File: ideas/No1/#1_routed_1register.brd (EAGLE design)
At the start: 110.2 x 90.1 mm, 20 parts, among them P1-O8RIGHT TD627832A, P1-P8LEFT TD627832A, U1 SN74HC595N, U2 SN74HC595N, U3 SN74HC595N

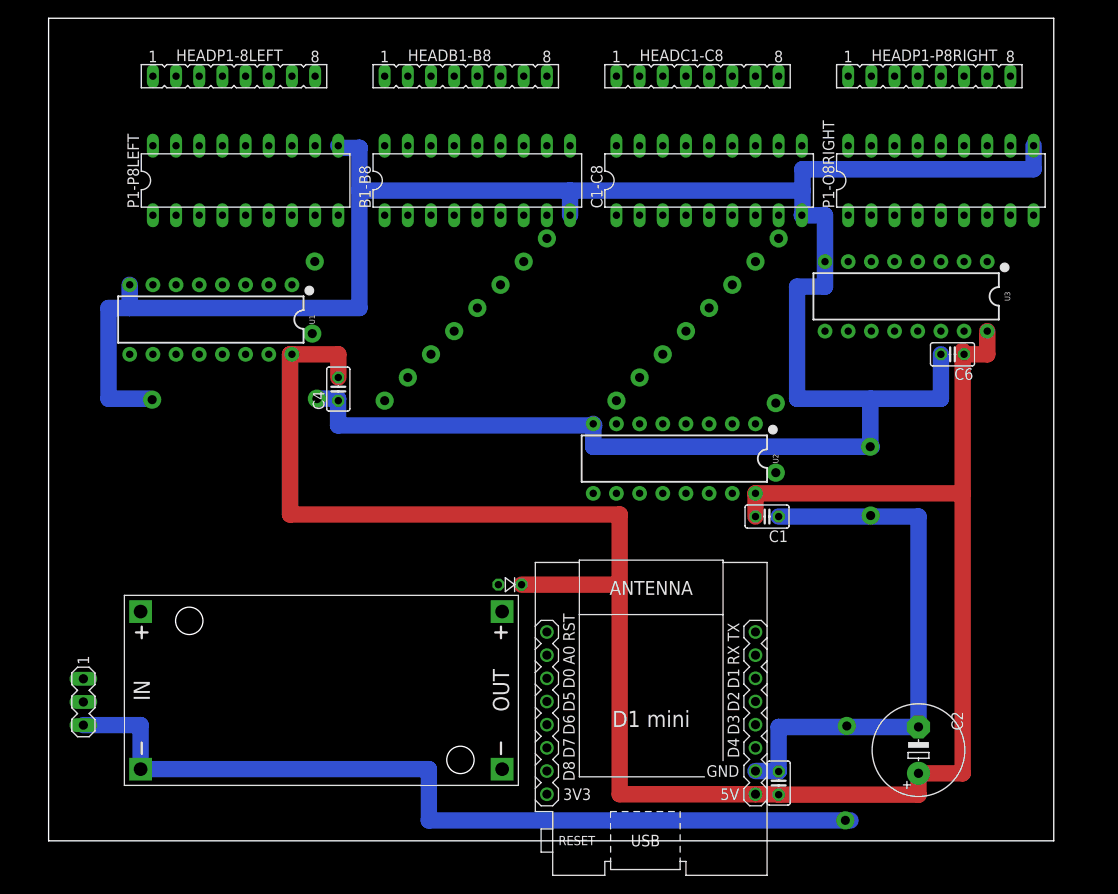
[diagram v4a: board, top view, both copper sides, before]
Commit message: 1_route_1register.sch changed
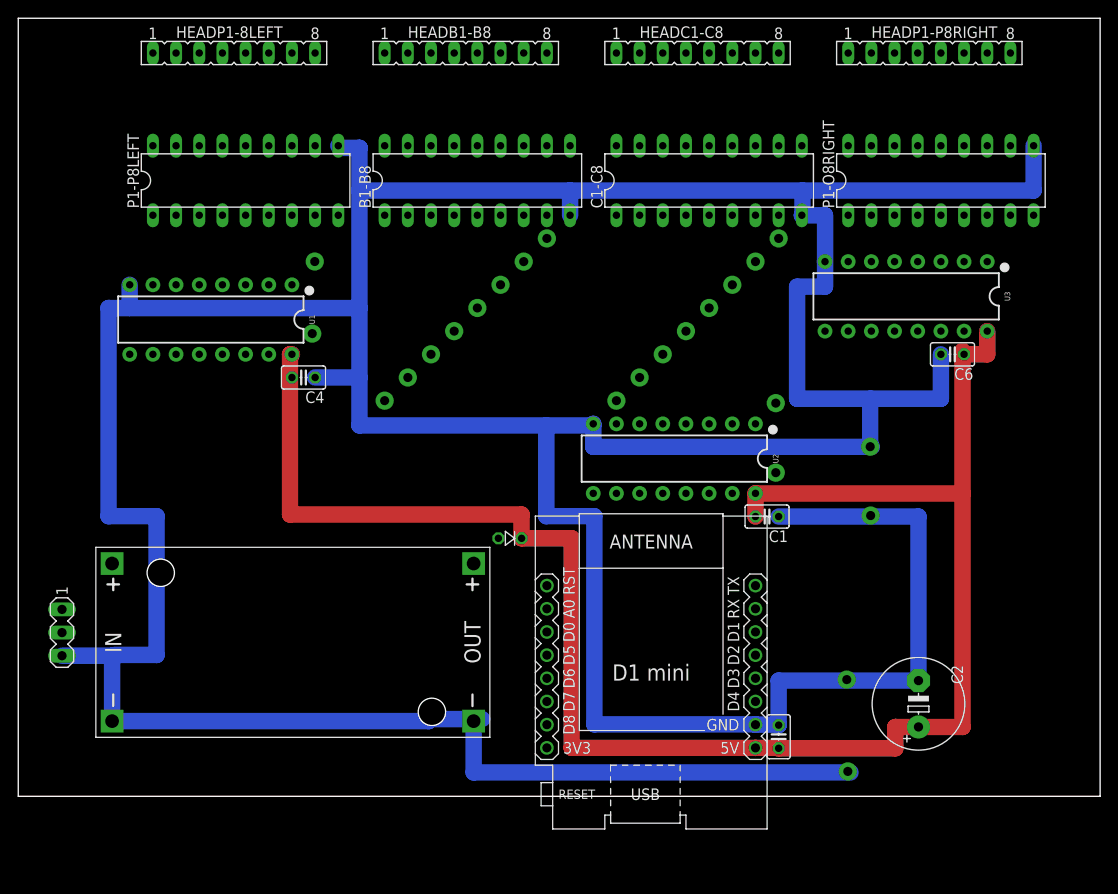
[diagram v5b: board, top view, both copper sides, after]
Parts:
- moved SV1 7.96 mm to (-67.1, 16.5)
- moved U$2 6.12 mm to (-41.8, 15.4)
- moved C2 5.08 mm to (26.8, 8.69)
- moved C3 5.08 mm to (11.4, 5.08)
- moved U$1 5.08 mm to (-2.54, 12.1)
- moved 1N4007 5.08 mm to (-18.0, 26.8)
- moved C4 4.02 mm to (-40.6, 44.5), turned to 180 degrees
- moved HEADB1-B8 2.54 mm to (-22.9, 80.0)
- moved HEADC1-C8 2.54 mm to (2.54, 80.0)
- moved HEADP1-8LEFT 2.54 mm to (-48.3, 80.0)
- moved HEADP1-P8RIGHT 2.54 mm to (27.9, 80.0)
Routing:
- net GND: track 289.5 -> 463.9 mm
- net N$36: track 83.2 -> 13.0 mm, vias 9 -> 4
- net N$61: track 94.5 -> 53.3 mm
- net VCC: track 219.5 -> 191.0 mm
- net N$70: track 0.00 -> 18.3 mm, vias 0 -> 3
- net 24V: track 97.0 -> 85.1 mm
- net N$76: track 81.3 -> 76.2 mm
- net N$74: track 76.2 -> 71.1 mm
- net N$80: track 38.1 -> 33.0 mm
- net N$60: track 33.0 -> 27.9 mm
- net N$37: track 25.4 -> 20.3 mm
- net N$34: track 68.5 -> 63.5 mm
- net N$9: track 7.62 -> 10.2 mm
- net N$59: track 7.62 -> 10.2 mm
- net N$58: track 7.62 -> 10.2 mm
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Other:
- board size 110.2 x 90.1 mm -> 118.6 x 85.3 mm
